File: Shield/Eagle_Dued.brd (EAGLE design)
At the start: 119.9 x 99.8 mm, 76 parts, among them IC1 7805TV, IC2 LM340MP-05

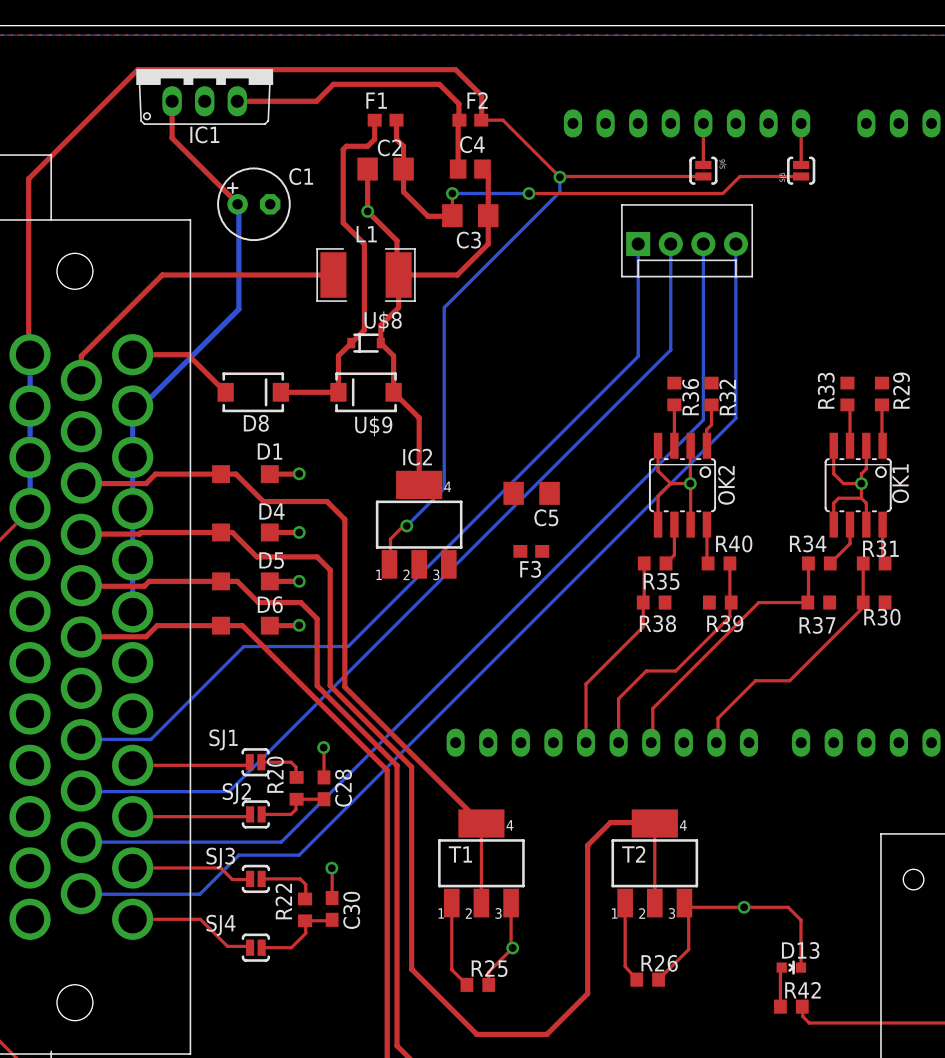
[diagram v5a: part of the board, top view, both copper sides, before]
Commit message: Updated canbus board to fix a layout issue, updated DueD to use DC/DC converter
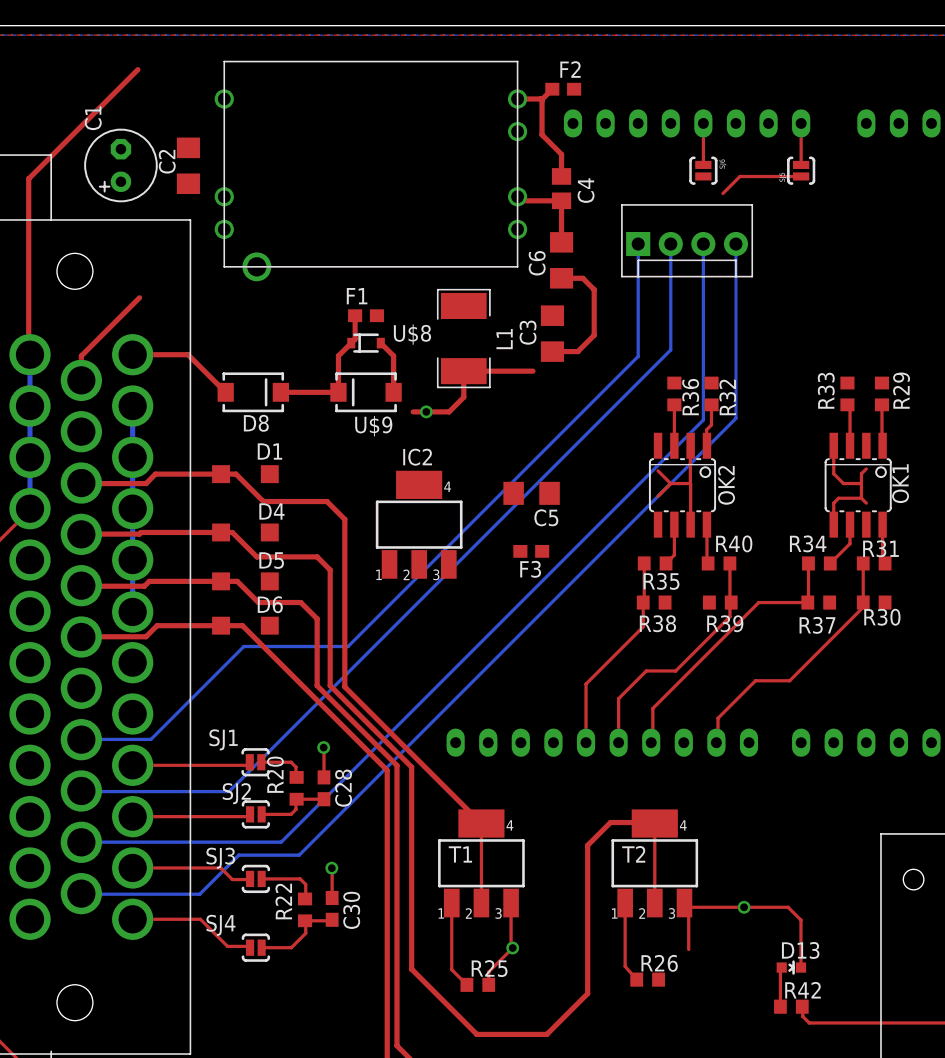
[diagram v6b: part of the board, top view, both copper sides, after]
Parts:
- removed IC1: 7805TV, linear:TO220V
- added C6: .01uF, rcl:C1206
- added U$1: CC3-E, dc-dc-converter:CC3-E
- C4: value .33uF -> 2uF
- moved C2 15.4 mm to (17.9, 88.9), turned to 270 degrees
- moved F1 15.3 mm to (31.8, 77.2)
- moved C3 11.2 mm to (46.3, 75.8), turned to 270 degrees
- moved C1 10.8 mm to (12.6, 88.9), turned to 90 degrees
- moved L1 9.09 mm to (39.4, 75.4), turned to 270 degrees
- moved F2 7.63 mm to (47.1, 94.9)
- moved C4 7.27 mm to (47.0, 87.1), turned to 270 degrees
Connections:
- new net EXTGND: C1.-, C2.2, C3.2, C6.1, D1.A, D4.A, D5.A, D6.A, OK1.2, OK1.4, OK1.5, OK1.7, OK2.2, OK2.4, OK2.5, OK2.7, R25.2, R26.2, R27.2, R28.2, T1.3, T2.3, T3.3, T4.3, U$1.P$2, U$1.P$3, U$3.14, U$3.7, U$8.2, U$9.A
- net +12V: now also U$1.P$1; no longer IC1.1
- net GND: now also C6.2, U$1.P$5; no longer C1.-, C2.2, C3.2, D1.A, D4.A, D5.A, D6.A, IC1.2, OK1.2, OK1.4, OK1.5, OK1.7, OK2.2, OK2.4, OK2.5, OK2.7, R25.2, R26.2, R27.2, R28.2, T1.3, T2.3, T3.3, T4.3, U$3.14, U$3.7, U$8.2, U$9.A
- net N$6: now also U$1.P$7; no longer IC1.3
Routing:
- net +5V: track 186.9 -> 102.5 mm, vias 2 -> 0
- net GND: track 158.8 -> 74.4 mm, vias 18 -> 9
- net +12V: track 85.7 -> 22.7 mm, vias 2 -> 0
- net EXTGND: track 0.00 -> 54.9 mm, vias 0 -> 3
- net N$3: track 29.2 -> 11.0 mm
- net DGND: track 24.2 -> 8.31 mm
- net N$6: track 23.6 -> 9.74 mm

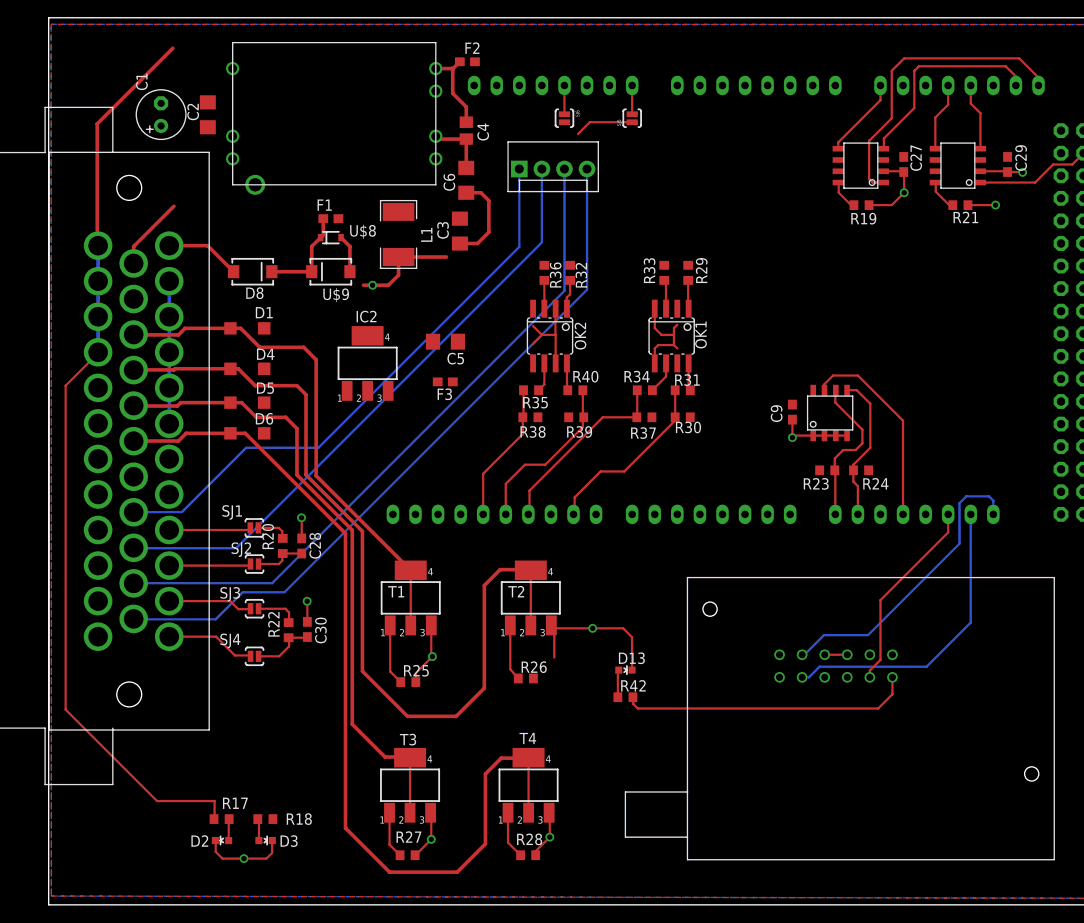
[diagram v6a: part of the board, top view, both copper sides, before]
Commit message: Added optocouplers to mosfet outputs
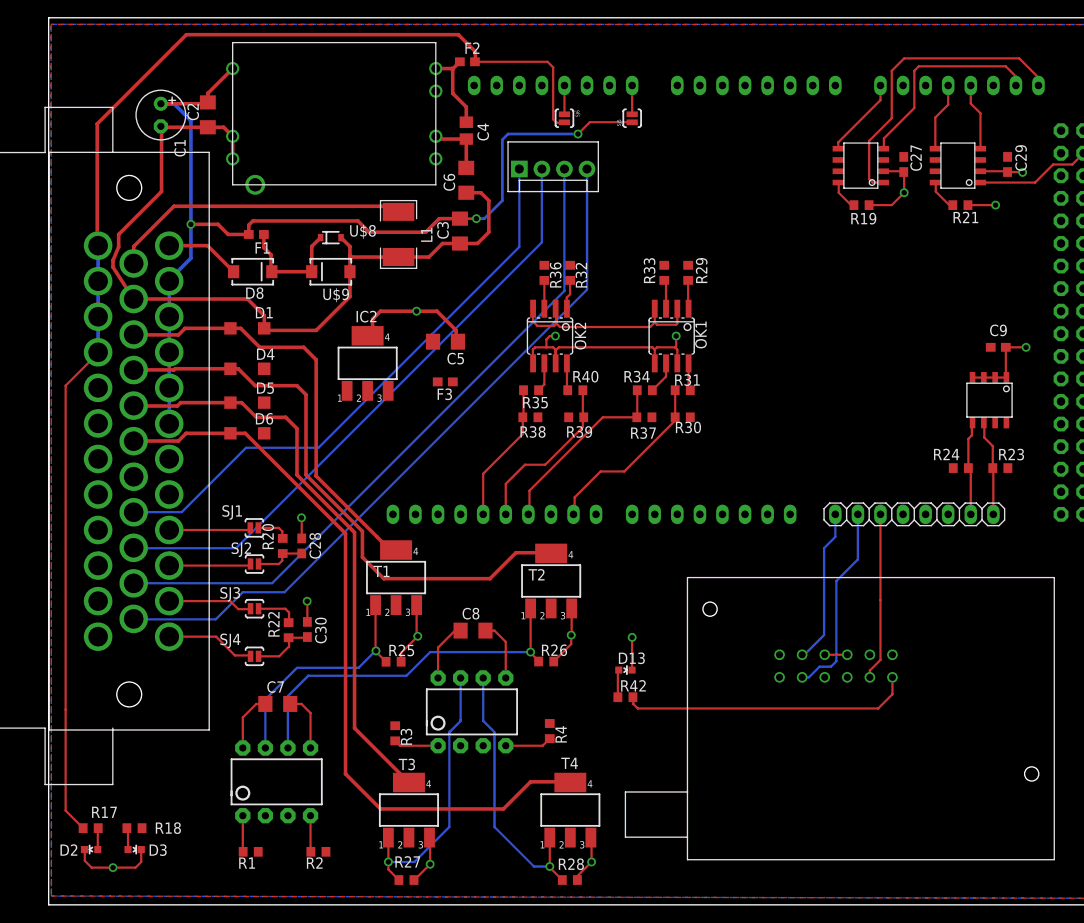
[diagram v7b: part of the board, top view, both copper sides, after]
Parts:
- added C7, C8: .1uF, rcl:C1206
- added R1, R2, R3, R4: 560, rcl:R0603
- added U$10, U$7: SFH6731, ck_custom:DIP8
- moved C9 24.3 mm to (106.9, 62.7), turned to 0 degrees
- moved U$5 23.6 mm to (108.4, 58.7), turned to 180 degrees
- moved R23 19.5 mm to (107.1, 49.1), turned to 180 degrees
- moved D2 14.8 mm to (4.78, 6.22)
- moved D3 14.8 mm to (9.68, 6.22)
- moved R18 14.8 mm to (9.65, 8.64)
- moved R17 14.8 mm to (4.72, 8.64)
- moved R24 11.2 mm to (102.6, 49.1), turned to 0 degrees
- moved F1 8.57 mm to (23.4, 75.4), turned to 180 degrees
- moved R28 5.47 mm to (58.6, 2.79)
- moved T4 5.47 mm to (58.7, 10.7)
- moved R26 2.98 mm to (56.0, 27.4)
- moved T2 2.98 mm to (56.5, 36.4)
- moved R25 2.82 mm to (38.8, 27.4)
- moved T1 2.82 mm to (39.1, 36.8)
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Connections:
- new net 0V: C7.2, C8.2, OK1.2, OK1.4, OK2.2, OK2.4, U$10.5, U$7.5
- new net MDRIVE1: R25.1, T1.1, U$10.7
- new net MDRIVE2: R26.1, T2.1, U$10.6
- new net MDRIVE3: R27.1, T3.1, U$7.7
- new net MDRIVE4: R28.1, T4.1, U$7.6
- new net N$10: R2.2, U$10.4
- new net N$11: R4.2, U$7.4
- new net N$5: R3.2, U$7.1
- new net N$7: R1.2, U$10.1
- net +12V: now also C7.1, C8.1, U$10.8, U$7.8
- net DIGOUT1: now also R1.1; no longer R25.1, T1.1
- net DIGOUT2: now also R2.1; no longer R26.1, T2.1
- net DIGOUT3: now also R3.1; no longer R27.1, T3.1
- net DIGOUT4: now also R4.1; no longer R28.1, T4.1
- net EXTGND: now also L1.P$2; no longer OK1.2, OK1.4, OK1.5, OK1.7, OK2.2, OK2.4, OK2.5, OK2.7
- net GND: now also OK1.5, OK1.7, OK2.5, OK2.7, U$10.2, U$10.3, U$7.2, U$7.3; no longer L1.P$2
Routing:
- net +12V: track 22.7 -> 124.0 mm, vias 0 -> 3
- net EXTGND: track 54.9 -> 116.9 mm, vias 3 -> 4
- net +5V: track 102.5 -> 146.7 mm
- net MDRIVE2: track 0.00 -> 41.5 mm, vias 0 -> 1
- net 0V: track 0.00 -> 38.5 mm
- net MDRIVE3: track 0.00 -> 31.0 mm, vias 0 -> 1
- net MDRIVE4: track 0.00 -> 30.7 mm, vias 0 -> 1
- net MOSFET2: track 95.9 -> 65.6 mm
- net MDRIVE1: track 0.00 -> 27.0 mm
- net DGND: track 8.31 -> 33.8 mm
- net RXD1: track 22.6 -> 0.00 mm
- net GND: track 74.4 -> 93.5 mm, vias 9 -> 11
- net MOSFET4: track 100.8 -> 84.2 mm
- net TXD3: track 33.3 -> 17.5 mm
- net RXD3: track 33.7 -> 22.1 mm
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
